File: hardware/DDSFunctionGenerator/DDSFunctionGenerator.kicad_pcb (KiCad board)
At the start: 2 copper layers, 80 x 65 mm, 145 parts, among them J1 Conn_Coaxial, J2 USB_B_Micro, J3 DG128-5.0-02P-14-00A, J4 DG128-5.0-02P-14-00A, J5 Conn_Coaxial, J6 Conn_Coaxial, J7 Conn_01x04_Male, J8 Conn_01x02_Female, Q1 Q_NPN_BEC, Q2 Q_NPN_BEC, Q3 Q_NPN_BEC, SW1 Rotary_Encoder_Switch, T1 Transformer_1P_1S, U1 TC1107-3.3VOA, U2 L7805, U3 L7805, U4 AD9832, U5 STM32F030K6Tx, U6 FT200XD, U7 AD8325, U8 MCP3425A0T-ECH, X1 XO91, Y1 Crystal

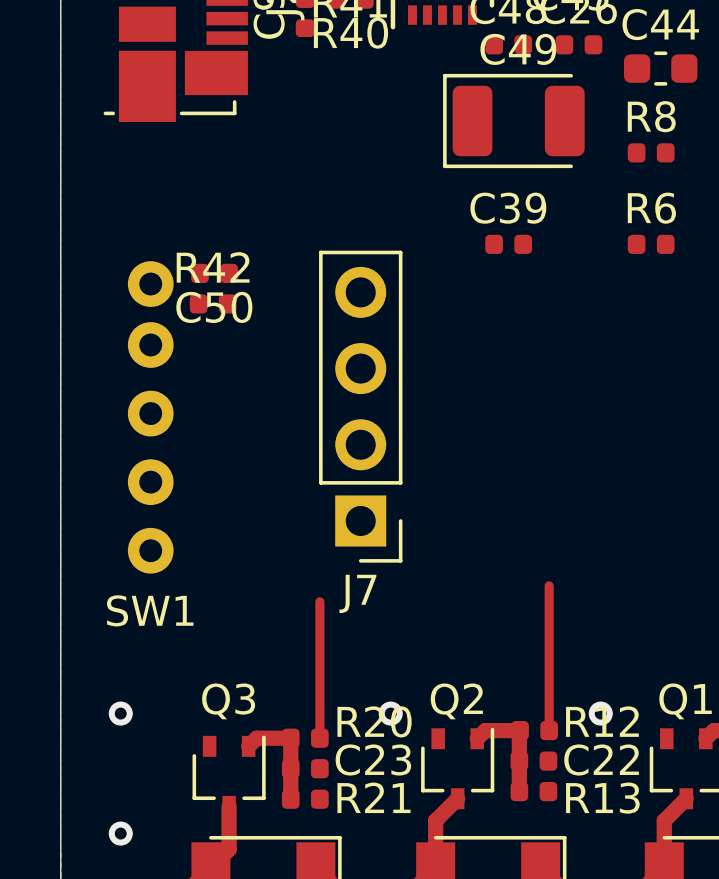
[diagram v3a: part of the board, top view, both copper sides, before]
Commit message: added missing changes for encoder footprint
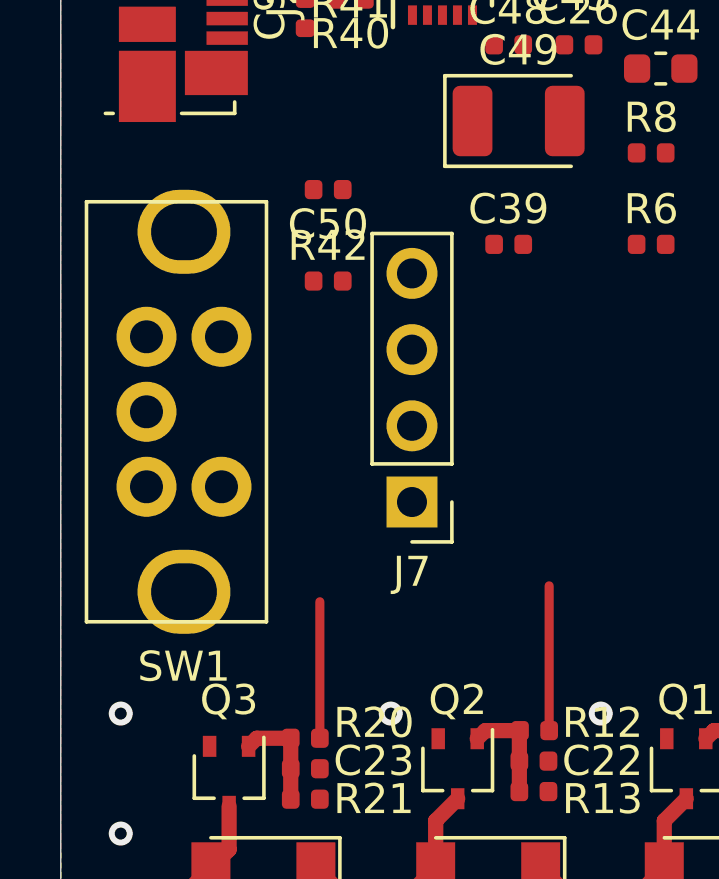
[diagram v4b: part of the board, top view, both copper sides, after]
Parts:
- SW1: value Rotary_Encoder_Switch -> EN11-VSB1AQ15
- moved SW1 5.23 mm to (70.4, 91.4)
- moved C50 4.71 mm to (73.9, 81.5)
- moved R42 3.91 mm to (73.9, 84.6)
- moved J7 1.82 mm to (76.7, 91.9)
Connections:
- R42 pad 2: (no net) -> Net-(R42-Pad2)
- R6 pad 2: (no net) -> Net-(R6-Pad2)
- R8 pad 2: (no net) -> Net-(R8-Pad2)
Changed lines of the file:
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@@
     (zones 0)
     (modules 145)
-    (nets 81)
+    (nets 84)
   )
   (page A4)
@@
   (net 79 "Net-(C1-Pad2)")
   (net 80 "Net-(C33-Pad1)")
+  (net 81 "Net-(R6-Pad2)")
+  (net 82 "Net-(R8-Pad2)")
+  (net 83 "Net-(R42-Pad2)")
   (net_class Default "This is the default net class."
     (clearance 0.127)
@@
     (uvia_drill 0.1)
   )
+  (module DDSFunctionGenerator:EN11-VNB1BQ15 (layer F.Cu)
+    (at 70.358 91.44 180)
+    (fp_text reference SW1 (at 1.25 -6) (layer F.SilkS)
+      (effects (font (size 1 1) (thickness 0.15)))
+    )
+    (fp_text value EN11-VSB1AQ15 (at 1.25 -7) (layer F.Fab)
+      (effects (font (size 1 1) (thickness 0.15)))
+    )
+    (fp_line (start -1.5 -4.5) (end 4.5 -4.5) (layer F.SilkS) (width 0.12))
+    (fp_line (start -1.5 9.5) (end -1.5 -4.5) (layer F.SilkS) (width 0.12))
+    (fp_line (start 4.5 9.5) (end -1.5 9.5) (layer F.SilkS) (width 0.12))
+    (fp_line (start 4.5 -4.5) (end 4.5 9.5) (layer F.SilkS) (width 0.12))
+    (pad GND thru_hole oval (at 1.25 8.5 180) (size 3.1 2.8) (drill oval 2.2 1.9) (layers *.Cu *.Mask)
+      (net 6 GND))
+    (pad GND thru_hole oval (at 1.25 -3.5 180) (size 3.1 2.8) (drill oval 2.2 1.9) (layers *.Cu *.Mask)
+      (net 6 GND))
+    (pad D thru_hole circle (at 0 5 180) (size 2 2) (drill 1.1) (layers *.Cu *.Mask)
+      (net 16 5V_DIGITAL))
+    (pad E thru_hole circle (at 0 0 180) (size 2 2) (drill 1.1) (layers *.Cu *.Mask)
+      (net 83 "Net-(R42-Pad2)"))
+    (pad C thru_hole circle (at 2.5 2.5 180) (size 2 2) (drill 1.1) (layers *.Cu *.Mask)
+      (net 16 5V_DIGITAL))
+    (pad A thru_hole circle (at 2.5 0 180) (size 2 2) (drill 1.1) (layers *.Cu *.Mask)
+      (net 81 "Net-(R6-Pad2)"))
+    (pad B thru_hole circle (at 2.5 5 180) (size 2 2) (drill 1.1) (layers *.Cu *.Mask)
+      (net 82 "Net-(R8-Pad2)"))
+    (model ${KIPRJMOD}/3DModels/EN11-VNB1BQ15.step
+      (at (xyz 0 0 0))
+      (scale (xyz 1 1 1))
+      (rotate (xyz 0 0 0))
+    )
+  )
   (module Resistor_SMD:R_1206_3216Metric (layer F.Cu)
     (at 108.458 120.65 270)
@@
   )
   (module Capacitor_SMD:C_0402_1005Metric (layer F.Cu)
-    (at 70.127 84.328 180)
+    (at 73.914 81.534 180)
     (descr "Capacitor SMD 0402 (1005 Metric), square (rectangular) end terminal, IPC_7351 nominal, (Body size source: http://www.tortai-tech.com/upload/download/2011102023233369053.pdf), generated with kicad-footprint-generator")
     (tags capacitor)
@@
   )
   (module Resistor_SMD:R_0402_1005Metric (layer F.Cu)
-    (at 70.081 85.344)
+    (at 73.914 84.582)
     (descr "Resistor SMD 0402 (1005 Metric), square (rectangular) end terminal, IPC_7351 nominal, (Body size source: http://www.tortai-tech.com/upload/download/2011102023233369053.pdf), generated with kicad-footprint-generator")
     (tags resistor)
@@
     (fp_line (start -0.5 -0.25) (end 0.5 -0.25) (layer F.Fab) (width 0.1))
     (fp_line (start -0.5 0.25) (end -0.5 -0.25) (layer F.Fab) (width 0.1))
-    (pad 2 smd roundrect (at 0.485 0) (size 0.59 0.64) (layers F.Cu F.Paste F.Mask) (roundrect_rratio 0.25))
+    (pad 2 smd roundrect (at 0.485 0) (size 0.59 0.64) (layers F.Cu F.Paste F.Mask) (roundrect_rratio 0.25)
+      (net 83 "Net-(R42-Pad2)"))
     (pad 1 smd roundrect (at -0.485 0) (size 0.59 0.64) (layers F.Cu F.Paste F.Mask) (roundrect_rratio 0.25)
       (net 65 ROT_S))
@@
     (fp_line (start -0.5 -0.25) (end 0.5 -0.25) (layer F.Fab) (width 0.1))
     (fp_line (start -0.5 0.25) (end -0.5 -0.25) (layer F.Fab) (width 0.1))
-    (pad 2 smd roundrect (at 0.485 0) (size 0.59 0.64) (layers F.Cu F.Paste F.Mask) (roundrect_rratio 0.25))
+    (pad 2 smd roundrect (at 0.485 0) (size 0.59 0.64) (layers F.Cu F.Paste F.Mask) (roundrect_rratio 0.25)
+      (net 82 "Net-(R8-Pad2)"))
     (pad 1 smd roundrect (at -0.485 0) (size 0.59 0.64) (layers F.Cu F.Paste F.Mask) (roundrect_rratio 0.25)
       (net 63 ROT_B))
@@
     (fp_line (start -0.5 -0.25) (end 0.5 -0.25) (layer F.Fab) (width 0.1))
     (fp_line (start -0.5 0.25) (end -0.5 -0.25) (layer F.Fab) (width 0.1))
-    (pad 2 smd roundrect (at 0.485 0) (size 0.59 0.64) (layers F.Cu F.Paste F.Mask) (roundrect_rratio 0.25))
+    (pad 2 smd roundrect (at 0.485 0) (size 0.59 0.64) (layers F.Cu F.Paste F.Mask) (roundrect_rratio 0.25)
+      (net 81 "Net-(R6-Pad2)"))
     (pad 1 smd roundrect (at -0.485 0) (size 0.59 0.64) (layers F.Cu F.Paste F.Mask) (roundrect_rratio 0.25)
       (net 64 ROT_A))
@@
   )
   (module Connector_PinHeader_2.54mm:PinHeader_1x04_P2.54mm_Vertical (layer F.Cu)
-    (at 75 92.58 180)
+    (at 76.708 91.948 180)
     (descr "Through hole straight pin header, 1x04, 2.54mm pitch, single row")
     (tags "Through hole pin header THT 1x04 2.54mm single row")
@@
     )
   )
-  (module DDSFunctionGenerator:EN11-VNB1BQ15 (layer F.Cu)
-    (at 68 96.112 180)
-    (fp_text reference SW1 (at 0 0.5) (layer F.SilkS)
-      (effects (font (size 1 1) (thickness 0.15)))
-    )
-    (fp_text value Rotary_Encoder_Switch (at 0 -0.5) (layer F.Fab)
-      (effects (font (size 1 1) (thickness 0.15)))
-    )
-    (pad 5 thru_hole circle (at 0 11.43 180) (size 1.524 1.524) (drill 0.762) (layers *.Cu *.Mask))
-    (pad 4 thru_hole circle (at 0 9.398 180) (size 1.524 1.524) (drill 0.762) (layers *.Cu *.Mask))
-    (pad 3 thru_hole circle (at 0 7.112 180) (size 1.524 1.524) (drill 0.762) (layers *.Cu *.Mask))
-    (pad 2 thru_hole circle (at 0 4.826 180) (size 1.524 1.524) (drill 0.762) (layers *.Cu *.Mask))
-    (pad 1 thru_hole circle (at 0 2.54 180) (size 1.524 1.524) (drill 0.762) (layers *.Cu *.Mask))
-    (model ${KIPRJMOD}/3DModels/EN11-VNB1BQ15.step
-      (at (xyz 0 0 0))
-      (scale (xyz 1 1 1))
-      (rotate (xyz 0 0 0))
-    )
-  )
   (module Connector_Coaxial:BNC_Amphenol_B6252HB-NPP3G-50_Horizontal (layer F.Cu)
     (at 78.232 127 90)
@@
   (segment (start 122.89 117.371) (end 122.913 117.348) (width 0.3048) (layer F.Cu) (net 6) (status 30))
   (segment (start 122.89 121.92) (end 122.89 117.371) (width 0.3048) (layer F.Cu) (net 6) (status 30))
-  (segment (start 121.666 116.078) (end 121.666 100.219) (width 0.3048) (layer F.Cu) (net 16))
   (segment (start 102.009 114.841) (end 102.009 115.491) (width 0.3048) (layer F.Cu) (net 6) (status 30))
   (segment (start 102.009 115.491) (end 102.009 116.141) (width 0.3048) (layer F.Cu) (net 6) (status 30))
@@
   (segment (start 111.241 122.6675) (end 110.998 122.9105) (width 0.508) (layer F.Cu) (net 15) (status 30))
   (segment (start 112.649 122.6675) (end 111.241 122.6675) (width 0.508) (layer F.Cu) (net 15) (status 30))
+  (segment (start 121.666 116.078) (end 121.666 100.219) (width 0.3048) (layer F.Cu) (net 16))
   (segment (start 121.92 117.371) (end 121.943 117.348) (width 0.508) (layer F.Cu) (net 16) (status 30))
   (segment (start 121.666 117.625) (end 121.943 117.348) (width 0.3048) (layer F.Cu) (net 16) (status 20))

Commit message: further bom simplification
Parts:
- C43, C44: footprint Capacitor_SMD:C_0603_1608Metric -> Capacitor_SMD:C_0402_1005Metric
- D4: footprint LED_SMD:LED_0805_2012Metric -> LED_SMD:LED_0402_1005Metric
- moved J7 23.7 mm to (90.2, 72.4), turned to 270 degrees
- moved R6 12.5 mm to (73.2, 88.1), turned to 180 degrees
- moved R8 12.5 mm to (73.2, 85.1), turned to 180 degrees
- moved C48 12.4 mm to (73.1, 87.1), turned to 180 degrees
- moved R31 9.16 mm to (75.2, 71.1), turned to 180 degrees
- moved C50 7.66 mm to (73.2, 89.2)
- moved C39 7.31 mm to (73.2, 86.1), turned to 180 degrees
- moved C44 5.75 mm to (79.2, 77.5), turned to 270 degrees
- moved R42 5.64 mm to (73.2, 90.2), turned to 180 degrees
- moved C49 5.15 mm to (75.2, 78.5), turned to 180 degrees
- moved D4 4.62 mm to (77.2, 71.1), turned to 0 degrees
- moved C26 4.12 mm to (78.2, 77.5), turned to 270 degrees
- moved C43 3.77 mm to (79.2, 71.1)
- moved SW1 1.02 mm to (70.4, 90.4)
- moved R40 0.51 mm to (74.1, 75.2)
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
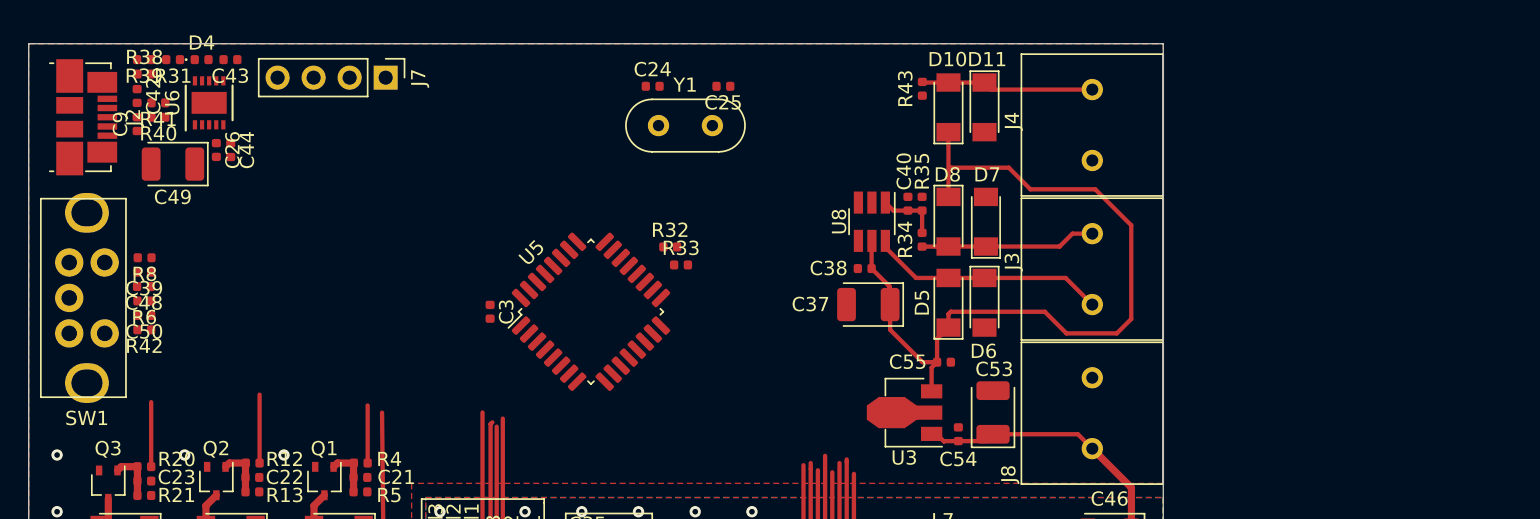
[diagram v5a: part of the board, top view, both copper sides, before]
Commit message: mcu pinout fix
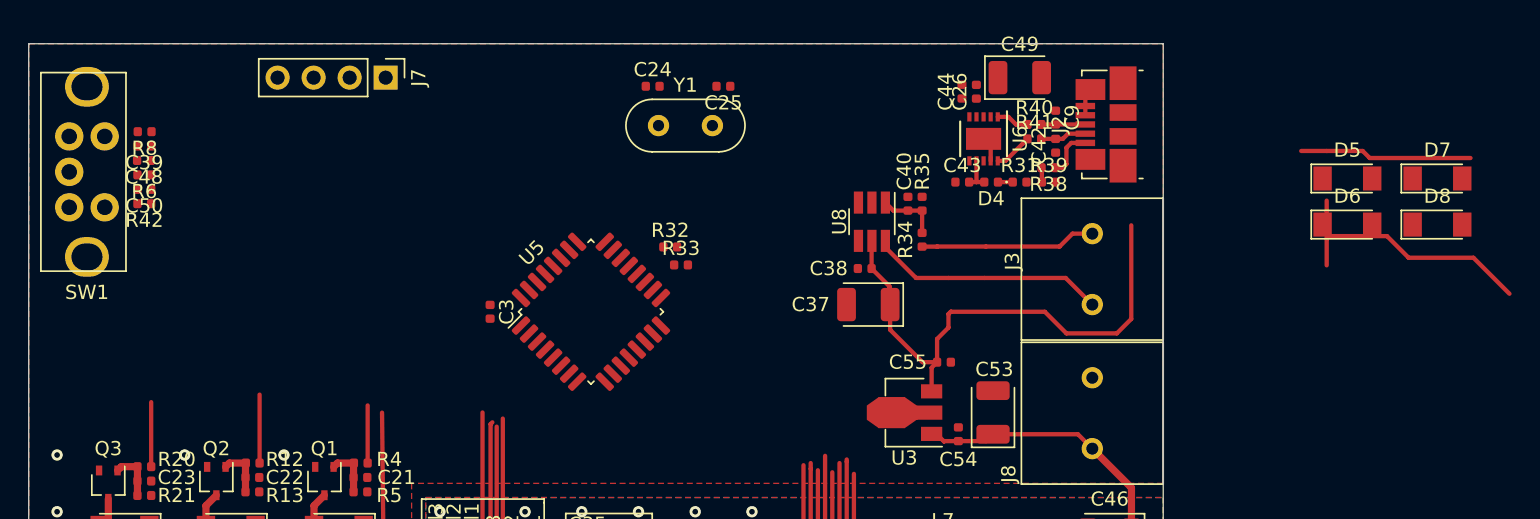
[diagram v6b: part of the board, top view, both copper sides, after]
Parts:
- removed D10, D11: D_Schottky, Diode_SMD:D_MiniMELF
- removed J4: DG128-5.0-02P-14-00A, DDSFunctionGenerator:DG128-5.0-02P-14-00A
- removed R43: 10R, Resistor_SMD:R_0402_1005Metric
- C37: value 47u -> 47u/6V3
- C49: value 47u/10V -> 47u/6V3
- D5, D6, D7, D8: value D_Schottky -> D
- L2, L3, L7, L9: value 4u7 -> 10u
- R37: value 50R -> 49R9
- moved J2 71.9 mm to (141.0, 75.7), turned to 90 degrees
- moved C42 64.9 mm to (137.4, 77.2), turned to 90 degrees
- moved C9 64.8 mm to (137.4, 75.2), turned to 270 degrees
- moved R39 64.4 mm to (136.9, 79.8), turned to 0 degrees
- moved R38 64.1 mm to (136.9, 78.7), turned to 180 degrees
- moved R41 61.8 mm to (135.9, 76.7), turned to 0 degrees
- moved R40 61.8 mm to (135.9, 75.7), turned to 0 degrees
- moved R31 60.3 mm to (134.9, 79.8), turned to 0 degrees
- moved C49 60.0 mm to (134.9, 72.4), turned to 0 degrees
- moved D4 56.3 mm to (132.9, 79.8), turned to 180 degrees
- moved U6 54.7 mm to (132.3, 76.7), turned to 270 degrees
- moved C26 53.8 mm to (131.8, 73.4), turned to 90 degrees
- moved C43 52.3 mm to (130.8, 79.8), turned to 0 degrees
- moved C44 51.7 mm to (130.8, 73.4), turned to 90 degrees
- moved D7 34.6 mm to (164.3, 79.5), turned to 0 degrees
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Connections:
- D6 pad 1: Net-(D5-Pad2) -> 5V_DIGITAL
- D6 pad 2: GND -> Net-(D6-Pad2)
- D7 pad 1: 5V_DIGITAL -> Net-(D5-Pad2)
- D7 pad 2: Net-(D7-Pad2) -> GND
- D8 pad 1: Net-(D7-Pad2) -> Net-(D6-Pad2)
- J3 pad 2: Net-(D7-Pad2) -> Net-(D6-Pad2)
- R34 pad 1: Net-(D7-Pad2) -> Net-(D6-Pad2)
- U5 pad 28: DIGITAL_OUT_1 -> (no net)
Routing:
- net Net-(D7-Pad2): track 12.4 -> 0.00 mm
- net Net-(D6-Pad2): track 0.00 -> 12.4 mm
- net GND: track 41.4 -> 45.1 mm
- net Net-(J2-Pad1): track 0.00 -> 3.52 mm
- net Net-(C42-Pad2): track 0.00 -> 3.26 mm
- net Net-(R41-Pad1): track 0.00 -> 3.21 mm
- net Net-(C9-Pad2): track 0.00 -> 3.11 mm
- net Net-(C43-Pad2): track 0.00 -> 2.56 mm
- net Net-(R40-Pad1): track 0.00 -> 2.32 mm
- net Net-(D4-Pad1): track 0.00 -> 1.04 mm
- net Net-(R38-Pad2): track 0.00 -> 1.03 mm

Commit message: minor improvements
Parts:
- removed J8: Conn_01x02_Female, DDSFunctionGenerator:DG128-5.0-02P-14-00A
- added C45: 47u/10V, Capacitor_Tantalum_SMD:CP_EIA-3528-21_Kemet-B, F.Cu at (133.1, 97.5)
- added C59: 100n, Capacitor_SMD:C_0402_1005Metric, F.Cu at (98.6, 80.5)
- added C60: 100n, Capacitor_SMD:C_0402_1005Metric, F.Cu at (101.5, 78.5)
- added C61: 100n, Capacitor_SMD:C_0402_1005Metric, F.Cu at (101.5, 80.5)
- added C62: 220u, Capacitor_SMD:CP_Elec_6.3x5.8, F.Cu at (115.8, 89.9)
- added J4: Conn_01x02_Female, DDSFunctionGenerator:DG128-5.0-02P-14-00A, F.Cu at (140.0, 99.1)
- added U9: GD25D10BOIGR, Package_SO:TSSOP-8_4.4x3mm_P0.65mm, F.Cu at (110.2, 78.2)
- C2: value 100n -> 47u/10V; footprint Capacitor_SMD:C_0402_1005Metric -> Capacitor_Tantalum_SMD:CP_EIA-3528-21_Kemet-B
- C24, C25: value 20p -> 8p
- C46, C53: value 47u/10V -> 100n; footprint Capacitor_Tantalum_SMD:CP_EIA-3528-21_Kemet-B -> Capacitor_SMD:C_0402_1005Metric
- U3: value L7805 -> L78L33_SO8; footprint Package_TO_SOT_SMD:SOT-89-3 -> Package_SO:SOIC-8_3.9x4.9mm_P1.27mm
- Y1: value Crystal -> 20MHz; footprint Crystal:Crystal_HC52-6mm_Vertical -> Oscillator:Oscillator_SMD_EuroQuartz_XO53-4Pin_5.0x3.2mm
- moved D7 37.5 mm to (128.0, 88.7), turned to 270 degrees
- moved C55 34.0 mm to (98.6, 78.5)
- moved D8 33.8 mm to (130.6, 83.1), turned to 90 degrees
- moved D5 28.9 mm to (130.6, 88.6), turned to 90 degrees
- moved D6 25.2 mm to (133.1, 86.9), turned to 90 degrees
- moved Y1 22.1 mm to (95.5, 93.0), turned to 180 degrees
- moved C6 5.74 mm to (142.8, 106.7), turned to 180 degrees
- moved C54 5.34 mm to (130.8, 92.2), turned to 0 degrees
- moved C46 4.19 mm to (137.2, 105.7), turned to 90 degrees
- moved C53 3.76 mm to (130.8, 99.1)
- moved C2 3.21 mm to (141.7, 104.1)
- moved U3 0.60 mm to (127.5, 96.5), turned to 270 degrees
- moved U2 0.57 mm to (141.7, 109.9)
- moved C27 0.51 mm to (94.0, 111.8)
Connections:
- C46 pad 1: 9V -> 5V_ANALOG
- C54 pad 1: 9V -> 5V_DIGITAL
- C6 pad 1: 5V_ANALOG -> 9V
- R12 pad 2: REL_2 -> (no net)
- R4 pad 2: REL_1 -> (no net)
- U3 pad 1: 9V -> 5V_DIGITAL
- U3 pad 3: 5V_DIGITAL -> GND
- U4 pad 7: SCLK -> SPI1_SCK
- U4 pad 8: SDATA -> SPI1_MOSI
- U5 pad 10: (no net) -> PSEL1
- U5 pad 11: (no net) -> SPI1_SCK
- U5 pad 12: (no net) -> SPI1_CS_AMPLIFIER
- U5 pad 13: (no net) -> SPI1_MOSI
- U5 pad 14: SCLK -> (no net)
- U5 pad 18: ROT_A -> FSELECT
- U5 pad 21: ROT_B -> ROT_A
- U5 pad 22: ROT_S -> ROT_B
- U5 pad 23: FSELECT -> ROT_S
- U5 pad 24: SDATA -> (no net)
- U5 pad 26: DATAEN -> (no net)
- U5 pad 27: TXEN -> (no net)
- U5 pad 29: PSEL1 -> (no net)
- U5 pad 30: PSEL0 -> (no net)
- U5 pad 6: REL_1 -> (no net)
- U5 pad 7: REL_3 -> (no net)
- U5 pad 8: REL_2 -> REL_3
- U5 pad 9: (no net) -> PSEL0
- U7 pad 1: DATAEN -> SPI1_CS_AMPLIFIER
- U7 pad 2: SDA -> SPI1_MOSI
- U7 pad 3: SCL -> SPI1_SCK
- U7 pad 6: TXEN -> Net-(C27-Pad1)
- U7 pad 7: GND -> Net-(C27-Pad1)
- Y1 pad 1: Net-(C24-Pad2) -> Net-(C25-Pad2)
- Y1 pad 2: Net-(C25-Pad2) -> GND
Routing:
- net SPI1_SCK: track 0.00 -> 39.9 mm
- net 5V_DIGITAL: track 76.0 -> 37.5 mm
- net SPI1_MOSI: track 0.00 -> 37.0 mm
- net SCLK: track 26.2 -> 0.00 mm
- net SDATA: track 23.7 -> 0.00 mm
- net TXEN: track 16.4 -> 0.00 mm
- net SCL: track 13.7 -> 0.00 mm
- net SDA: track 13.2 -> 0.00 mm
- net SPI1_CS_AMPLIFIER: track 0.00 -> 12.8 mm
- net DATAEN: track 12.8 -> 0.00 mm
- net Net-(D10-Pad2): track 12.1 -> 0.00 mm
- net 9V: track 63.9 -> 57.9 mm
- net GND: track 45.1 -> 42.9 mm
- net Net-(C27-Pad1): track 32.3 -> 33.0 mm
- net Net-(D6-Pad2): track 12.4 -> 13.1 mm
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
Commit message: further routing of mcu part
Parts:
- removed U9: GD25D10BOIGR, Package_SO:TSSOP-8_4.4x3mm_P0.65mm
- added C63: 100n, Capacitor_SMD:C_0402_1005Metric, F.Cu at (75.7, 73.7)
- added C64: 2u2, Capacitor_SMD:C_0402_1005Metric, B.Cu at (94.0, 99.6)
- added C65: 2u2, Capacitor_SMD:C_0402_1005Metric, B.Cu at (95.5, 99.5)
- added J8: Conn_01x04_Female, Connector_PinHeader_2.54mm:PinHeader_1x04_P2.54mm_Vertical, F.Cu at (94.5, 83.3)
- R33: footprint Resistor_SMD:R_0402_1005Metric -> Resistor_SMD:R_0805_2012Metric_Pad1.15x1.40mm_HandSolder
- moved C25 30.9 mm to (88.4, 90.4)
- moved C24 26.0 mm to (88.4, 88.9)
- moved C60 15.0 mm to (112.3, 88.9), turned to 270 degrees
- moved C3 13.7 mm to (111.3, 88.9)
- moved C61 12.6 mm to (99.6, 93.0), turned to 180 degrees
- moved J7 12.0 mm to (78.2, 73.7), turned to 90 degrees
- moved C55 9.02 mm to (97.1, 87.4)
- moved C59 6.08 mm to (97.0, 86.4)
- moved C62 3.37 mm to (116.8, 86.7), turned to 90 degrees
- moved C39 2.50 mm to (75.7, 77.2)
- moved C48 2.50 mm to (75.6, 78.2)
- moved C50 2.50 mm to (75.7, 80.3)
- moved R42 2.50 mm to (75.7, 81.3)
- moved R6 2.50 mm to (75.7, 79.2)
- moved R8 2.50 mm to (75.7, 76.2)
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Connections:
- R12 pad 2: (no net) -> REL_2
- R4 pad 2: (no net) -> REL_1
- U5 pad 10: PSEL1 -> PSEL0
- U5 pad 14: (no net) -> FSELECT
- U5 pad 18: FSELECT -> (no net)
- U5 pad 21: ROT_A -> (no net)
- U5 pad 22: ROT_B -> (no net)
- U5 pad 23: ROT_S -> (no net)
- U5 pad 26: (no net) -> ROT_B
- U5 pad 27: (no net) -> ROT_A
- U5 pad 28: (no net) -> ROT_S
- U5 pad 29: (no net) -> /Microcontroller/USART_TX
- U5 pad 30: (no net) -> /Microcontroller/USART_RX
- U5 pad 6: (no net) -> REL_3
- U5 pad 7: (no net) -> REL_2
- U5 pad 8: REL_3 -> REL_1
- U5 pad 9: PSEL0 -> PSEL1
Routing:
- net SCL: track 0.00 -> 92.2 mm, vias 0 -> 2
- net SDA: track 0.00 -> 67.0 mm, vias 0 -> 2
- net 9V: track 57.9 -> 108.3 mm
- net 5V_DIGITAL: track 37.5 -> 85.2 mm
- net SPI1_MOSI: track 37.0 -> 71.2 mm, vias 0 -> 2
- net SPI1_SCK: track 39.9 -> 71.3 mm, vias 0 -> 2
- net ROT_B: track 0.00 -> 31.0 mm
- net ROT_S: track 0.00 -> 29.9 mm
- net ROT_A: track 0.00 -> 29.9 mm
- net REL_3: track 4.55 -> 32.0 mm
- net REL_2: track 4.83 -> 24.4 mm
- net PSEL1: track 28.1 -> 46.1 mm
- net PSEL0: track 30.4 -> 47.7 mm
- net FSYNC: track 23.9 -> 40.7 mm, vias 0 -> 2
- net FSELECT: track 26.1 -> 42.7 mm, vias 0 -> 2
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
